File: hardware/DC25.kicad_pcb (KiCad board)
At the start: 2 copper layers, 101.6 x 55.9 mm, 28 parts, among them P1 CONN_01X04, P2 CONN_01X04, SW1 SW_DPDT_x2, U1 ATMEGA328P-AU, Y1 16MHz

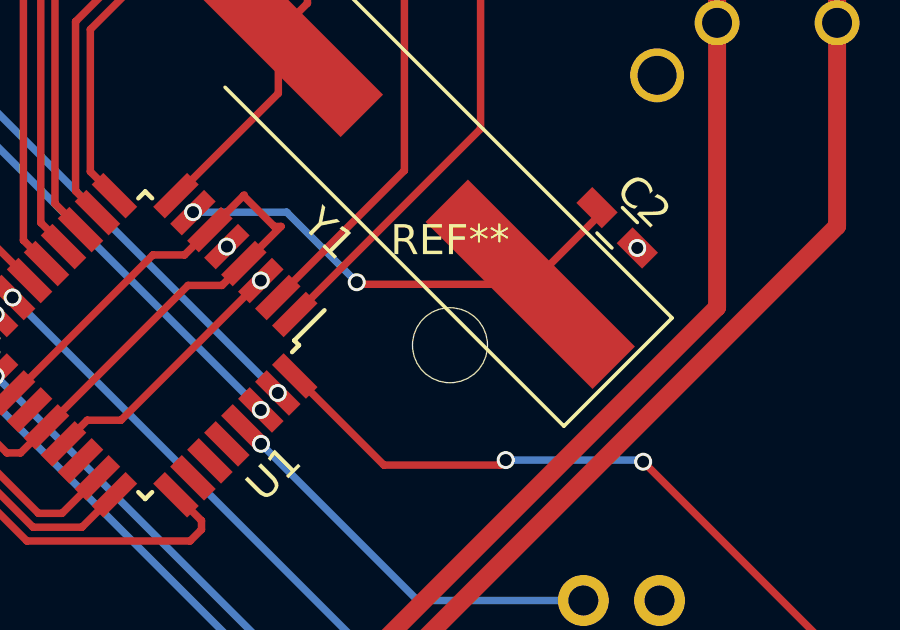
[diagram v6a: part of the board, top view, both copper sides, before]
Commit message: mode batter mounting down one notch
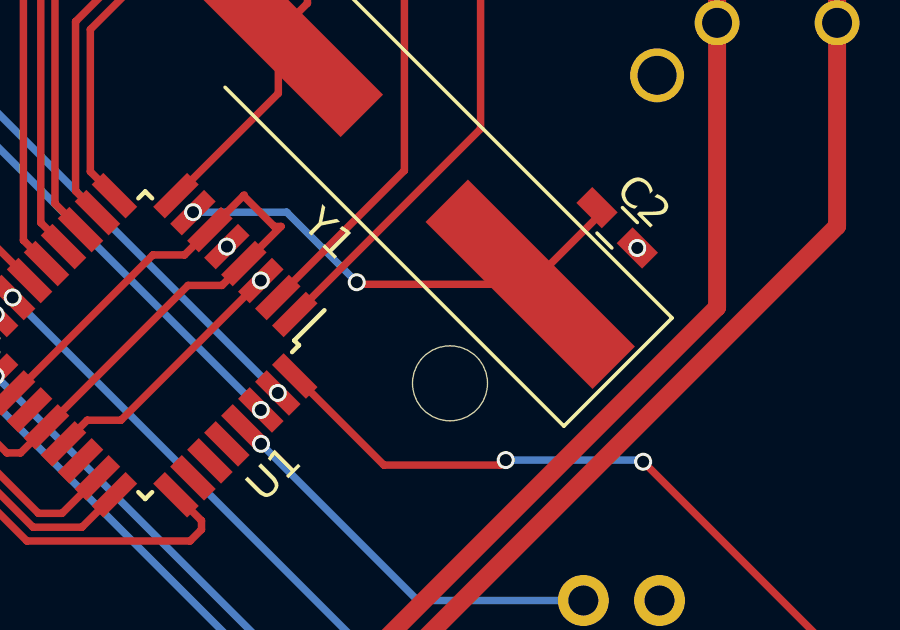
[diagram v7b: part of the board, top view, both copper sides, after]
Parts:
- moved REF** 1.27 mm to (64.4, 43.0)
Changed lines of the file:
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@@
     (links 69)
     (no_connects 0)
-    (area 13.514999 13.754999 115.265001 69.785001)
+    (area 11.898289 12.209 116.881711 71.401711)
     (thickness 1.6)
     (drawings 16)
@@
   )
   (module Mounting_Holes:MountingHole_2.5mm (layer F.Cu)
-    (at 64.39 41.77)
+    (at 64.39 43.04)
     (descr "Mounting Hole 2.5mm, no annular")
     (tags "mounting hole 2.5mm no annular")
-    (fp_text reference REF** (at 0 -3.5) (layer F.SilkS)
+    (fp_text reference REF** (at 0 -3.5) (layer F.SilkS) hide
       (effects (font (size 1 1) (thickness 0.15)))
     )
@@
     (effects (font (size 1.5 1.5) (thickness 0.3)))
   )
-  (gr_line (start 28.43 51.55) (end 100.43 51.55) (angle 90) (layer B.SilkS) (width 0.2))
-  (gr_line (start 100.43 31.55) (end 100.43 51.55) (angle 90) (layer B.SilkS) (width 0.2))
-  (gr_line (start 28.43 31.55) (end 28.43 51.55) (angle 90) (layer B.SilkS) (width 0.2))
-  (gr_line (start 28.43 31.55) (end 100.43 31.55) (angle 90) (layer B.SilkS) (width 0.2))
+  (gr_line (start 28.43 52.82) (end 100.43 52.82) (angle 90) (layer B.SilkS) (width 0.2))
+  (gr_line (start 100.43 32.82) (end 100.43 52.82) (angle 90) (layer B.SilkS) (width 0.2))
+  (gr_line (start 28.43 32.82) (end 28.43 52.82) (angle 90) (layer B.SilkS) (width 0.2))
+  (gr_line (start 28.43 32.82) (end 100.43 32.82) (angle 90) (layer B.SilkS) (width 0.2))
   (gr_line (start 13.59 64.63) (end 13.59 18.91) (angle 90) (layer Edge.Cuts) (width 0.15))
   (gr_line (start 110.11 69.71) (end 18.67 69.71) (angle 90) (layer Edge.Cuts) (width 0.15))
